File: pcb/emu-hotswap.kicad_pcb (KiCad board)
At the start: 2 copper layers, 157.8 x 118.3 mm, 76 parts, among them J1 TRRS, SW1 SW_Push, SW10 SW_Push, SW11 SW_Push, SW12 SW_Push, SW13 SW_Push, SW14 SW_Push, SW15 SW_Push, SW16 SW_Push, SW17 SW_Push, SW18 SW_Push, SW19 SW_Push, SW2 SW_Push, SW20 SW_Push, SW21 SW_Push, SW22 SW_Push, SW23 SW_Push, SW24 SW_Push, SW25 SW_Push, SW26 SW_Push, SW27 SW_Push, SW28 SW_Push, SW29 SW_Push, SW3 SW_Push, SW30 SW_Push, SW31 SW_Push, SW32 SW_Push, SW4 SW_Push, SW5 SW_Push, SW6 SW_Push, SW7 SW_Push, SW8 SW_Push, SW9 SW_Push, U1 ProMicro

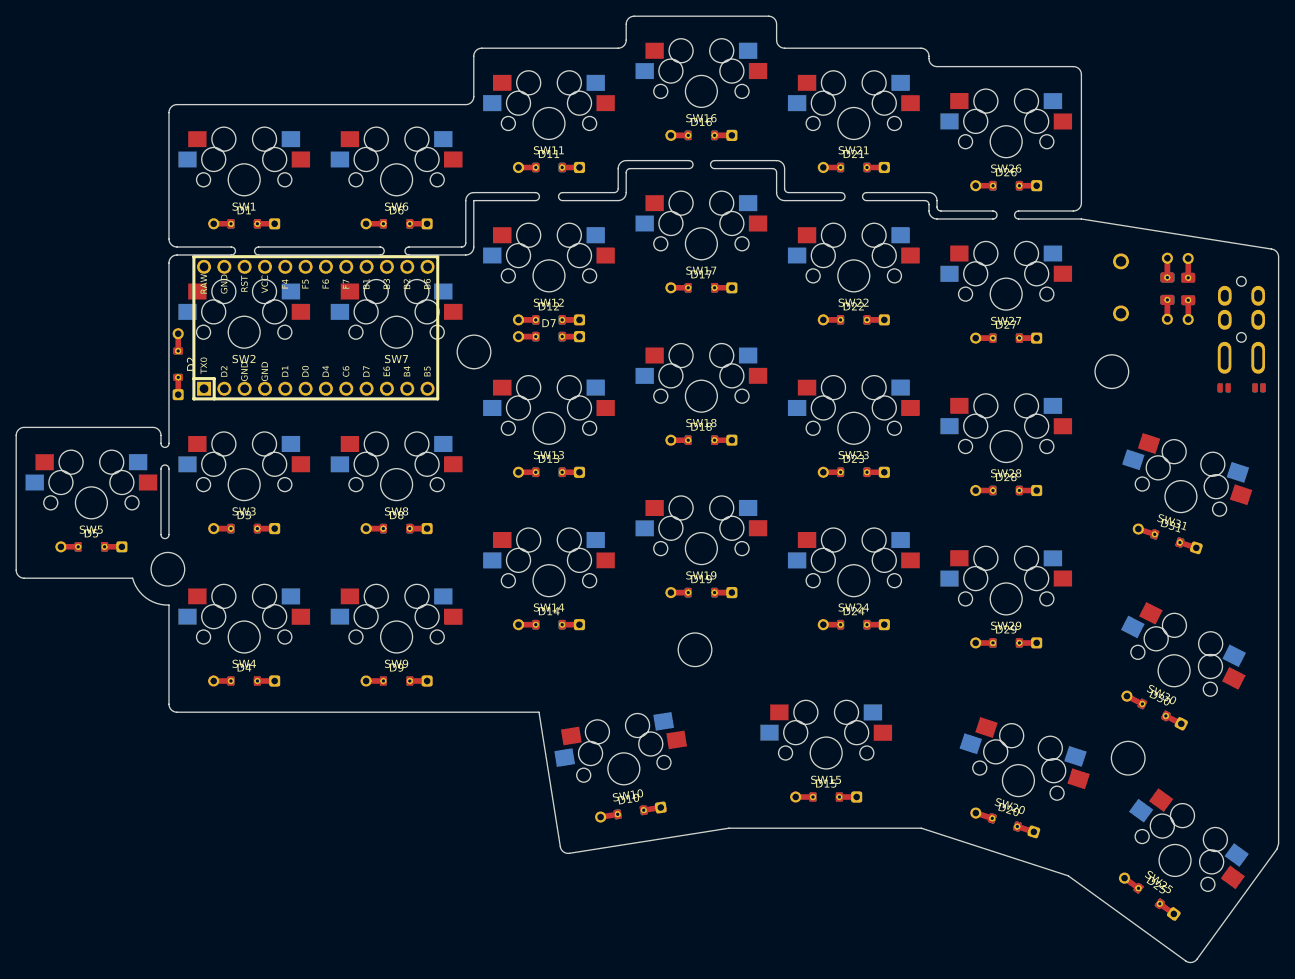
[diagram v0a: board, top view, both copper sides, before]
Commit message: Rotated thumb switches to 180 degrees.
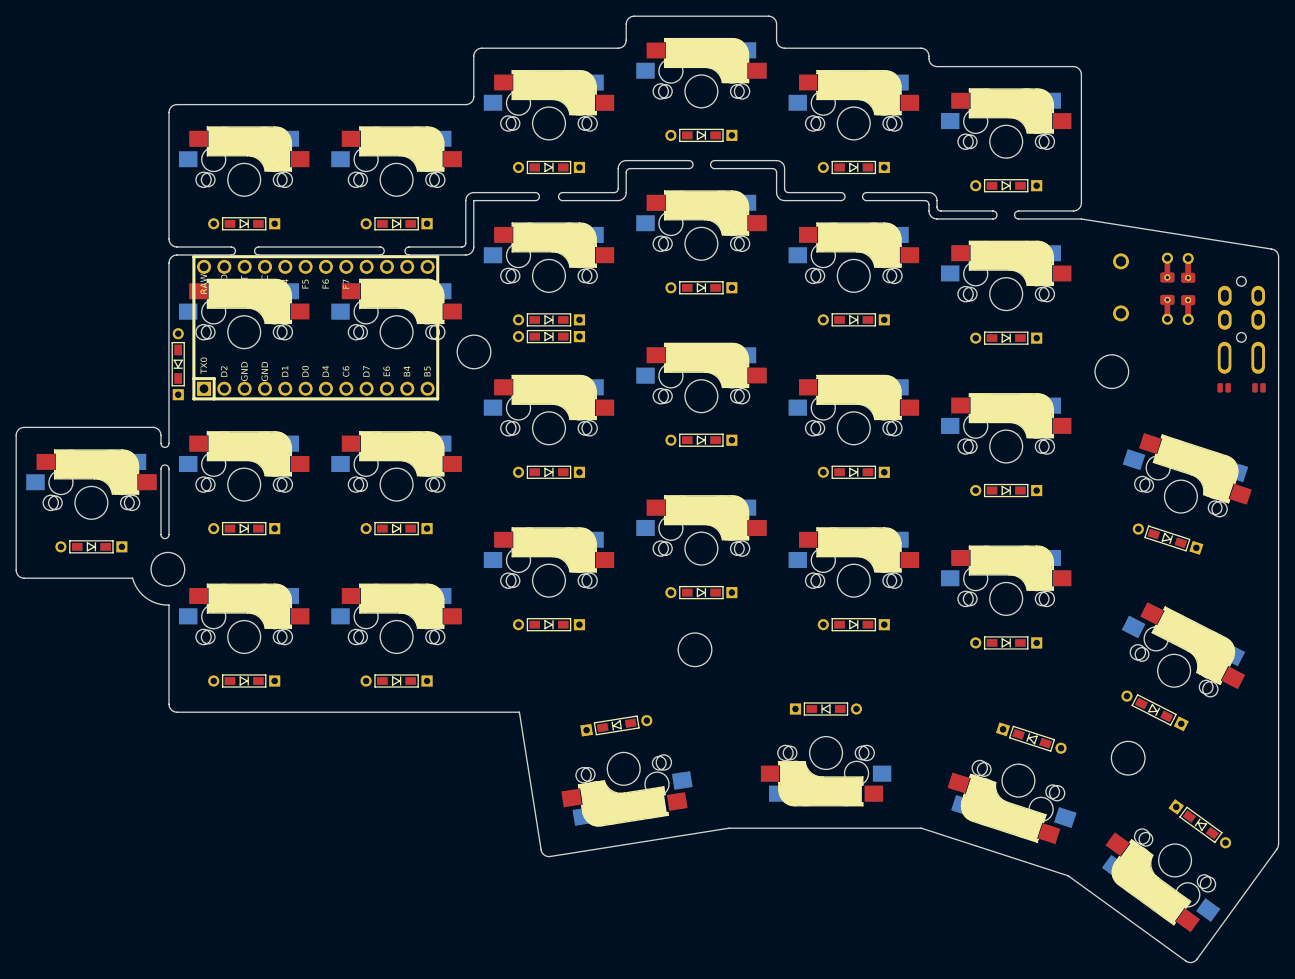
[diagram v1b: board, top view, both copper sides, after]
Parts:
- D1, D10, D11, D12, D13, D14, D15, D16, D17, D18, D19, D2, D20, D21, D22, D23, D24, D25, D26, D27, D28, D29, D3, D30, D31, D4, D5, D6, D7, D8, D9: footprint used_footprints:Diode_Hybrid_SOD-123 -> used_footprints:D3_TH_SMD
- SW1, SW11, SW12, SW13, SW14, SW16, SW17, SW18, SW19, SW2, SW20, SW21, SW22, SW23, SW24, SW25, SW26, SW27, SW28, SW29, SW3, SW30, SW31, SW4, SW5, SW6, SW7, SW8, SW9: footprint used_footprints:Switch_Mx_Hotswap_1u -> used_footprints:CherryMX_MidHeight_Hotswap_1u
- SW10, SW15: footprint used_footprints:Switch_Mx_Hotswap_1u -> used_footprints:CherryMX_MidHeight_Hotswap_1.25u
- moved D15 11.0 mm to (177.7, 117.2), turned to 0 degrees
- moved D10 11.0 mm to (151.6, 119.2), turned to 9 degrees
- moved D20 11.0 mm to (203.5, 120.9), turned to 342 degrees
- moved D25 11.0 mm to (224.6, 131.6), turned to 324 degrees
- turned SW10 to 9 degrees
- turned SW15 to 0 degrees
- turned SW20 to 342 degrees
- turned SW25 to 324 degrees
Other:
- outline, holes or cut-outs redrawn

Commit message: Routing...
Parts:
- added HM6: CaseHole, used_footprints:Hole_Mount_M4, F.Cu at (114.5, 98.6)
- moved JP3 0.11 mm to (231.8, 77.0)
- moved JP4 0.11 mm to (231.8, 77.0)
- moved JP1 0.07 mm to (227.6, 77.0)
- moved JP2 0.07 mm to (227.6, 77.0)
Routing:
- net GND: track 0.00 -> 171.5 mm, vias 0 -> 1
- net /rowF: track 0.00 -> 164.6 mm
- net SCL: track 0.00 -> 146.6 mm, vias 0 -> 1
- net SDA: track 0.00 -> 142.9 mm, vias 0 -> 1
- net VCC: track 0.00 -> 130.0 mm
- net /RST: track 0.00 -> 127.1 mm
- net /col0: track 0.00 -> 97.5 mm
- net /col5: track 0.00 -> 96.4 mm
- net /rowE: track 0.00 -> 94.2 mm
- net /col4: track 0.00 -> 78.9 mm
- net /rowB: track 0.00 -> 76.8 mm, vias 0 -> 1
- net /col3: track 0.00 -> 60.8 mm
- net /rowD: track 0.00 -> 57.4 mm
- net /rowC: track 0.00 -> 36.8 mm
- net Net-(D2-Pad2): track 0.00 -> 27.5 mm, vias 0 -> 1
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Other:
- outline, holes or cut-outs redrawn

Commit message: Routing...
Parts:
- moved HM4 1.03 mm to (162.3, 110.7)
- moved U1 0.50 mm to (113.5, 69.5)
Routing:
- net /col1: track 0.00 -> 45.9 mm, vias 0 -> 1
- net Net-(D7-Pad2): track 0.00 -> 44.0 mm, vias 0 -> 2
- net Net-(D12-Pad2): track 0.00 -> 31.8 mm, vias 0 -> 1
- net Net-(D11-Pad2): track 0.00 -> 28.4 mm
- net Net-(D6-Pad2): track 0.00 -> 28.3 mm
- net Net-(D21-Pad2): track 0.00 -> 28.3 mm
- net Net-(D16-Pad2): track 0.00 -> 28.3 mm
- net Net-(D27-Pad2): track 0.00 -> 28.2 mm
- net Net-(D22-Pad2): track 0.00 -> 28.1 mm
- net Net-(D1-Pad2): track 0.00 -> 28.0 mm
- net Net-(D26-Pad2): track 0.00 -> 28.0 mm
- net Net-(D17-Pad2): track 0.00 -> 27.8 mm
- net /rowA: track 22.7 -> 49.6 mm
- net /rowE: track 94.2 -> 119.9 mm
- net /col2: track 0.00 -> 25.5 mm
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
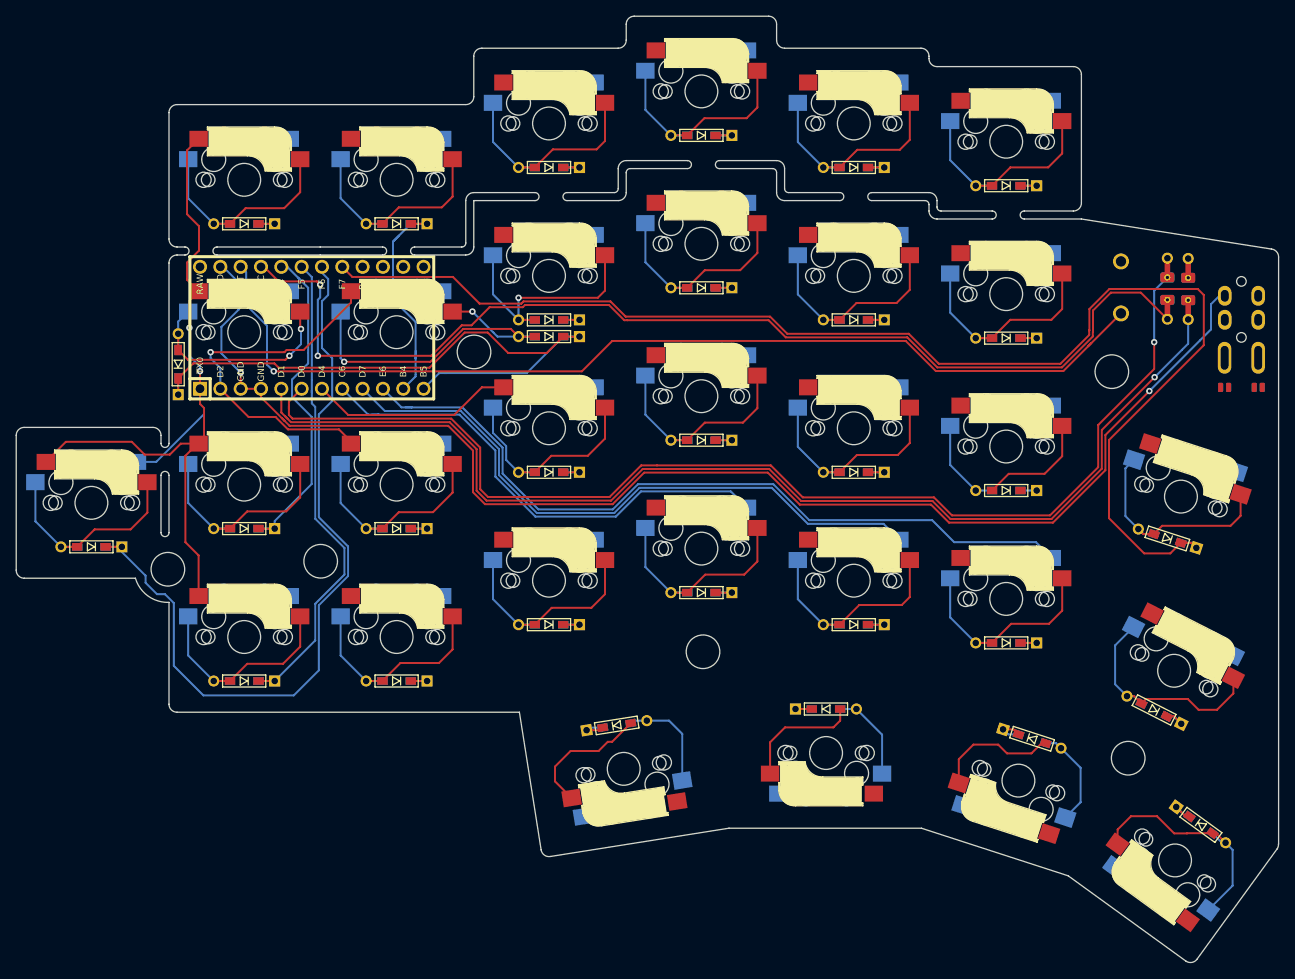
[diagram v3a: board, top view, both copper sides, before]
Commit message: All routes seems to be connected.
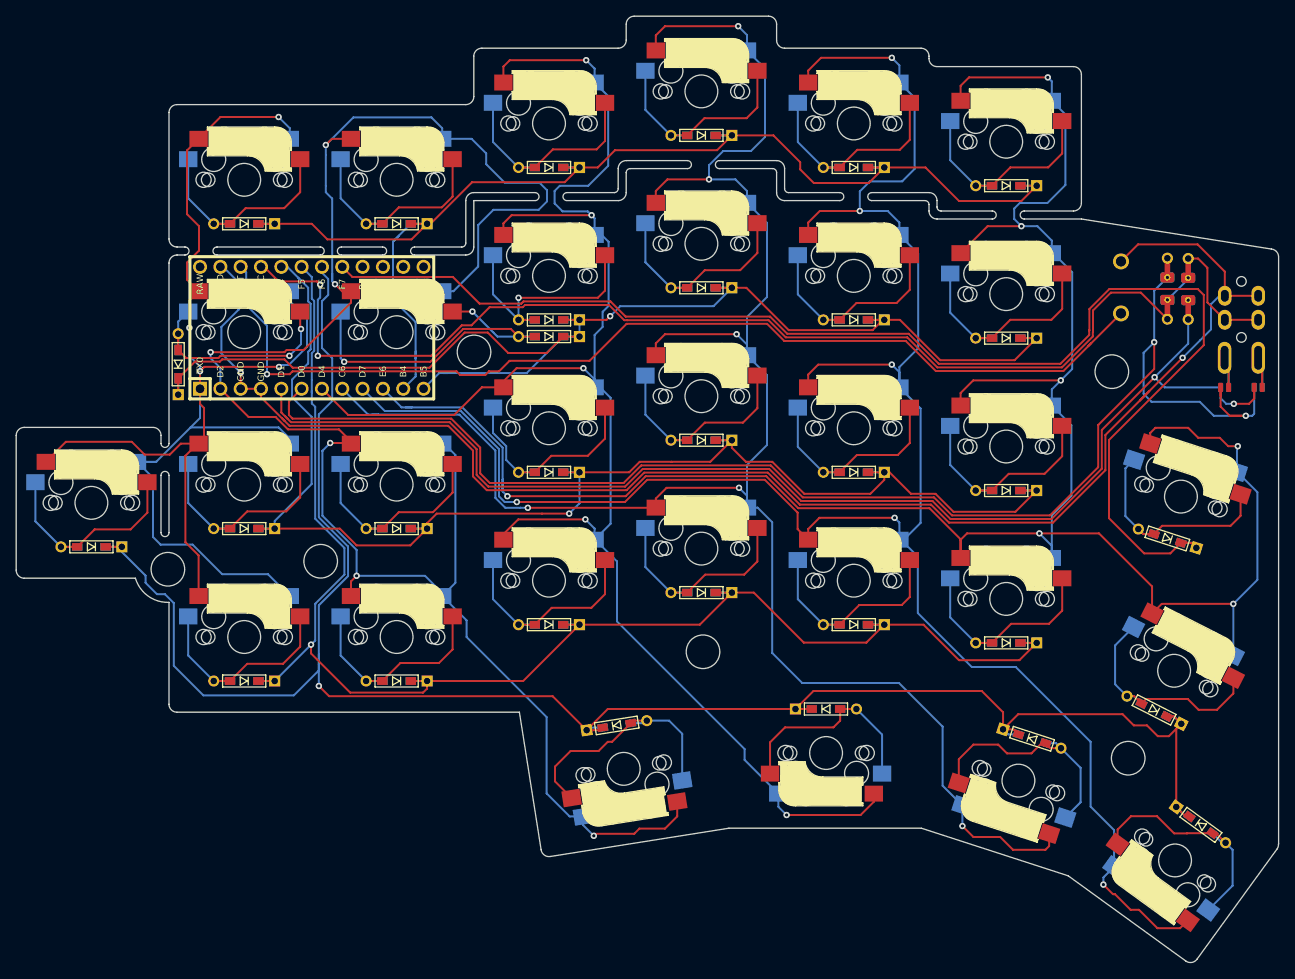
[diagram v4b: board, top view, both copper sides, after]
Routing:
- net /col4: track 80.2 -> 271.3 mm, vias 0 -> 6
- net /col5: track 97.7 -> 288.6 mm, vias 0 -> 7
- net /col1: track 45.9 -> 236.2 mm, vias 1 -> 6
- net /col3: track 62.1 -> 248.4 mm, vias 0 -> 6
- net /col2: track 25.5 -> 211.0 mm, vias 0 -> 5
- net /rowE: track 119.9 -> 252.4 mm, vias 0 -> 1
- net /rowC: track 61.7 -> 176.4 mm, vias 0 -> 1
- net /rowA: track 49.6 -> 157.4 mm
- net /rowD: track 82.2 -> 188.3 mm, vias 0 -> 1
- net /col0: track 96.4 -> 182.7 mm, vias 2 -> 4
- net /rowB: track 97.9 -> 165.2 mm, vias 0 -> 1
- net SCL: track 146.9 -> 181.5 mm, vias 1 -> 2
- net VCC: track 136.5 -> 159.7 mm
- net GND: track 172.8 -> 194.2 mm
- net SDA: track 143.5 -> 161.2 mm, vias 1 -> 2
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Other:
- outline, holes or cut-outs redrawn

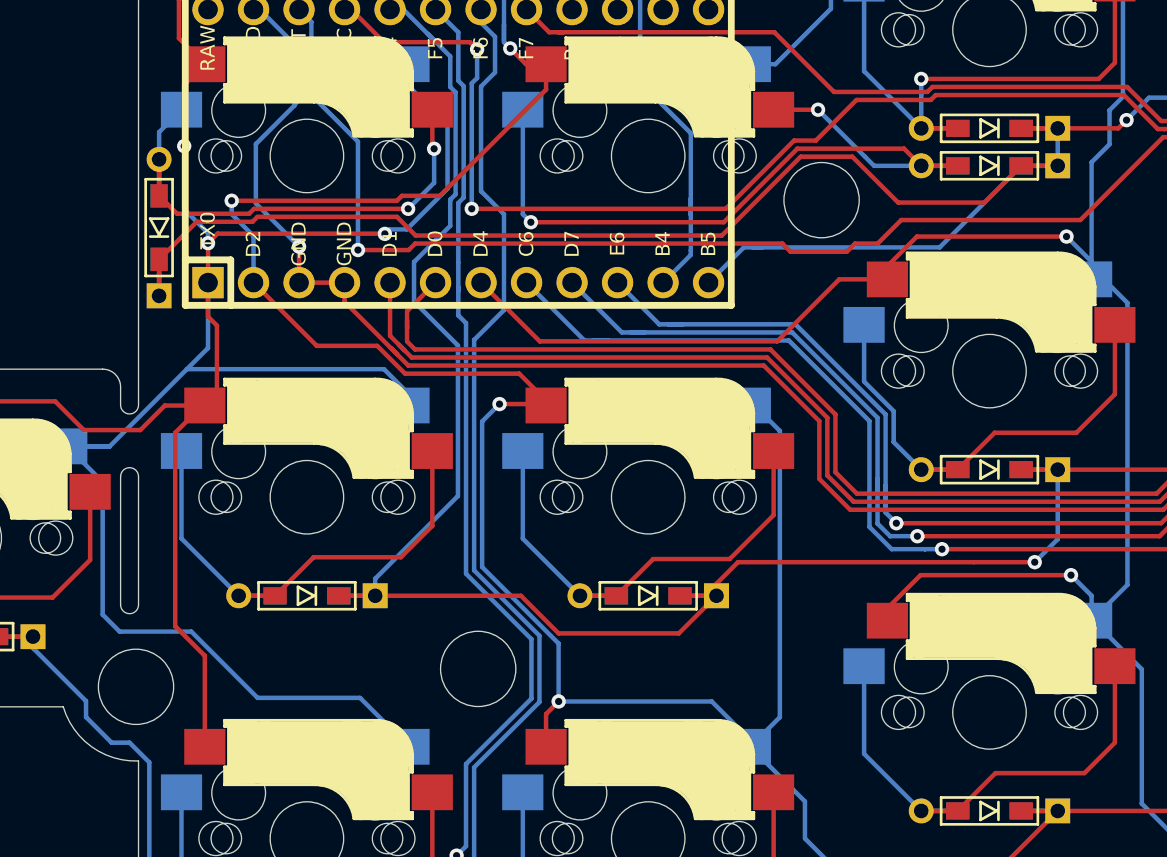
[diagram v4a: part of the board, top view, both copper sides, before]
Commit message: Moved diode a bit
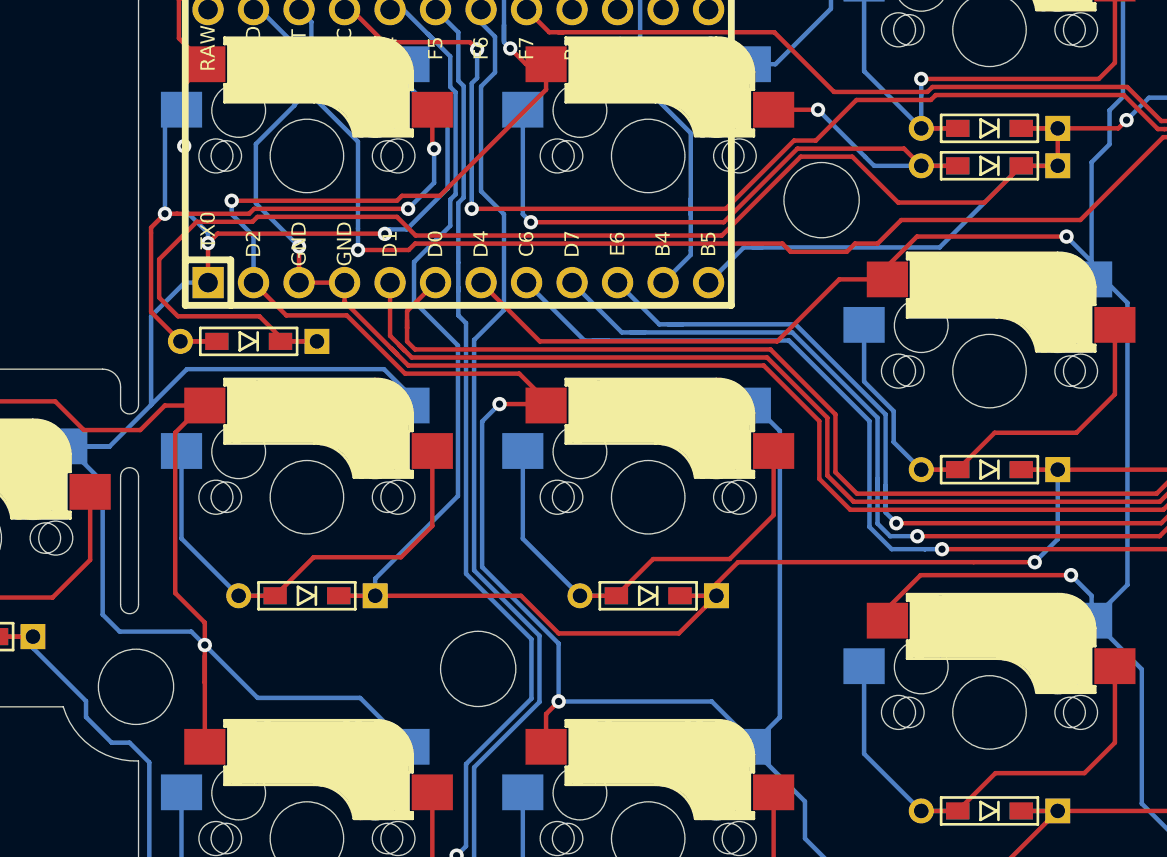
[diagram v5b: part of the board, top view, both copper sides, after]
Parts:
- moved D2 8.08 mm to (101.8, 80.4), turned to 180 degrees
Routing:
- net Net-(D2-Pad2): track 28.0 -> 38.2 mm, vias 2 -> 3
- net /rowB: track 165.2 -> 175.3 mm
- net /col0: track 182.7 -> 180.4 mm, vias 4 -> 5
